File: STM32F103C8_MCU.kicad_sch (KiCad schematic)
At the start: 12 parts, among them J1 Header Socket 1X5, SW1 SW_SPST, U1 STM32F103C8T6, Y1 Crystal

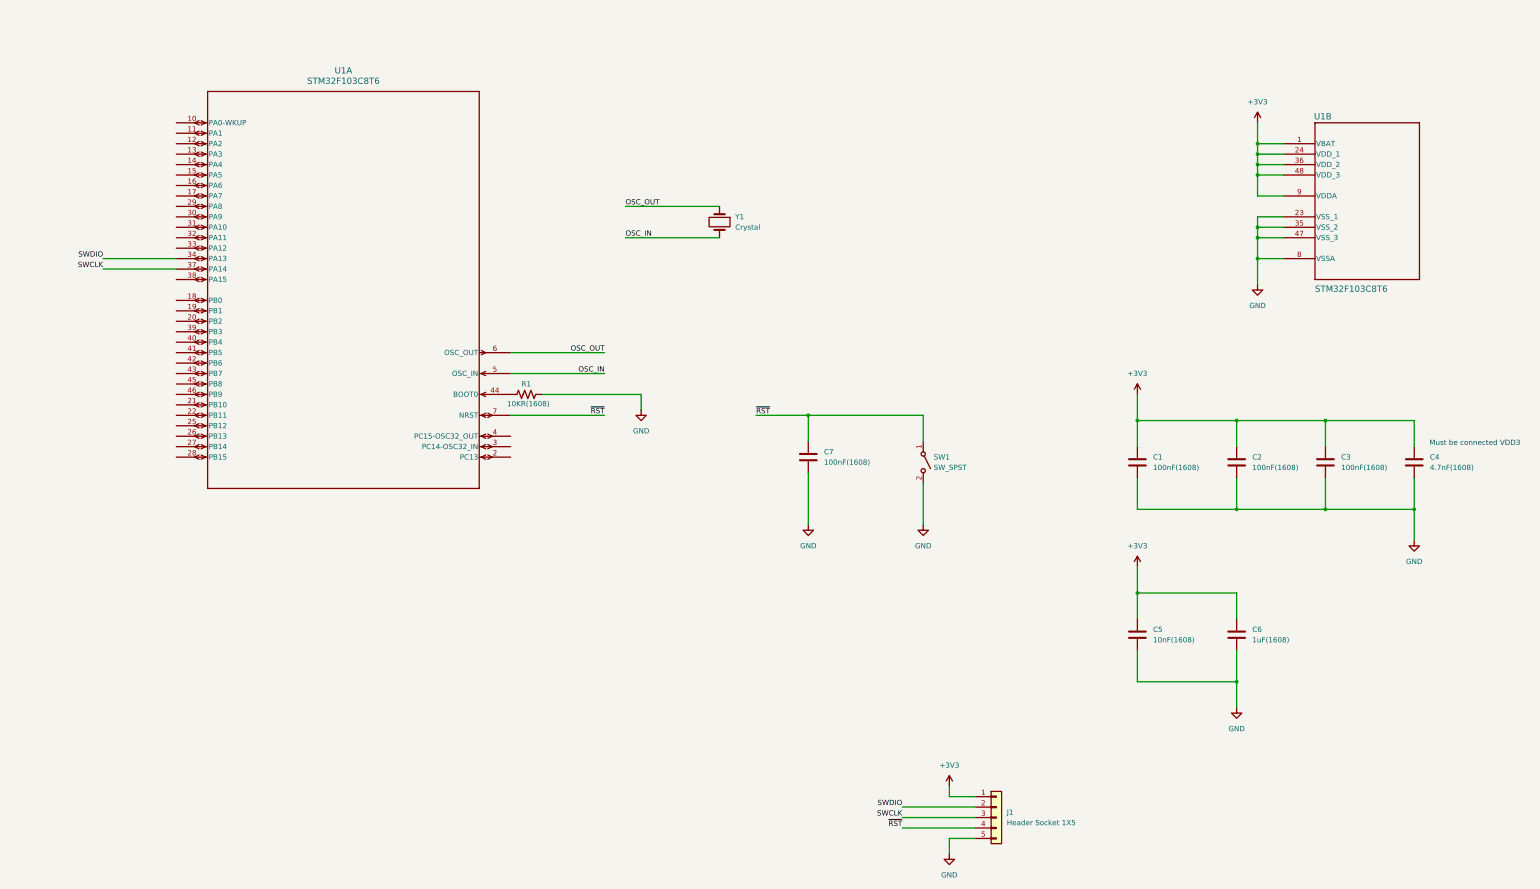
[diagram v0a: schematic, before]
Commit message: Update schematics and add LED circuit
- Add led.kicad_sch (new LED subcircuit)
- Update STM32F103C8_MCU schematic
- Update top-level schematic and project file
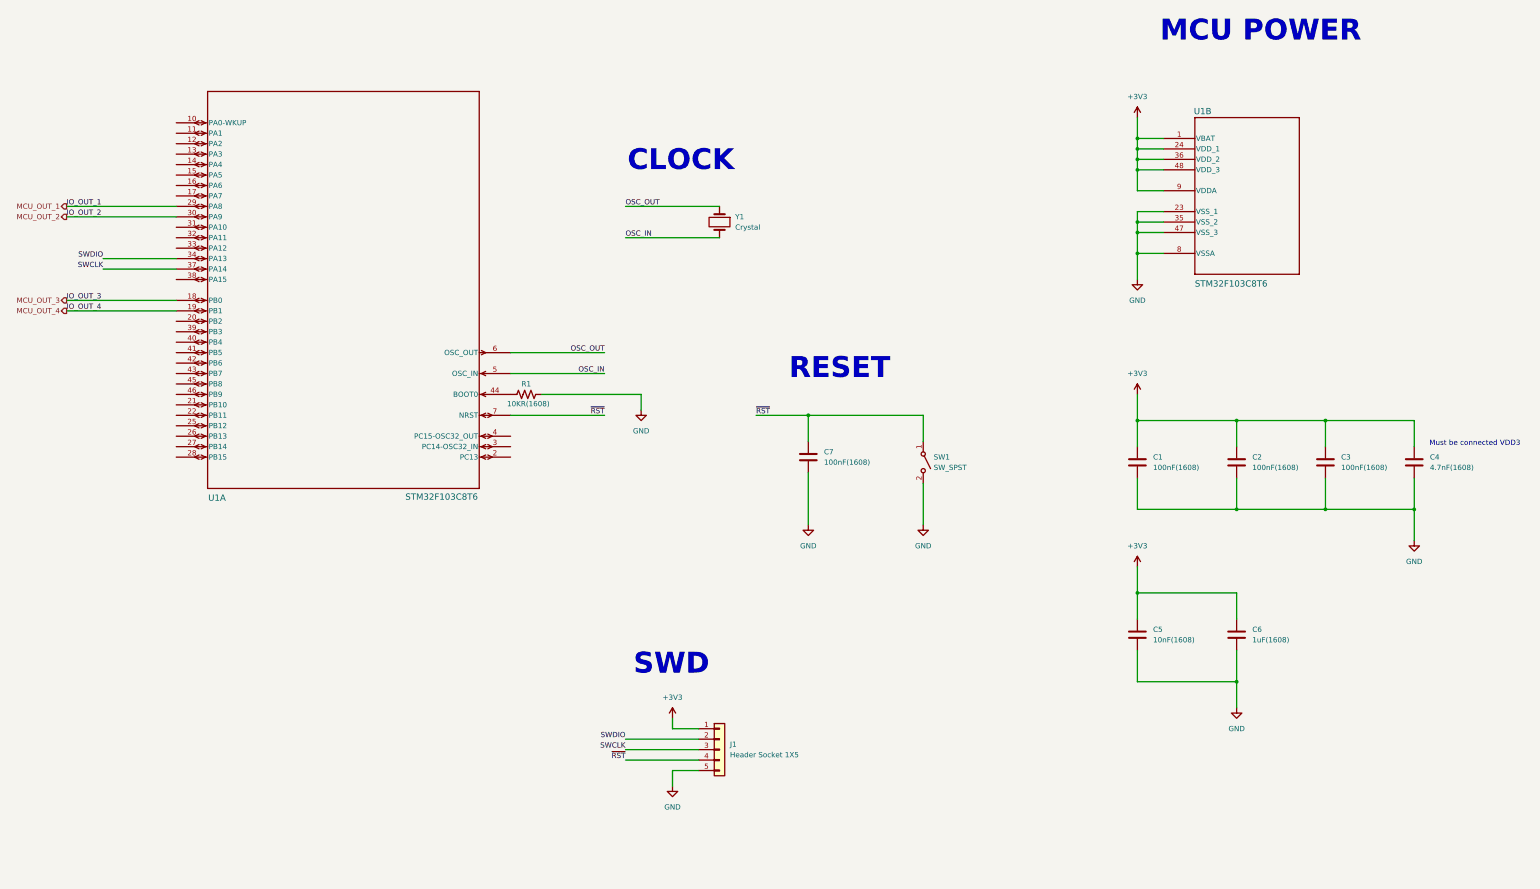
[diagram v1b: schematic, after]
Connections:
- net MCU_OUT_3: now reaches U1.18 (PB0)
- net MCU_OUT_4: now reaches U1.19 (PB1)
- net MCU_OUT_1: now reaches U1.29 (PA8)
- net MCU_OUT_2: now reaches U1.30 (PA9)
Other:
- note added: "CLOCK"
- note added: "MCU POWER"
- note added: "RESET"
- note added: "SWD"
- moved on the sheet: J1, U1B
